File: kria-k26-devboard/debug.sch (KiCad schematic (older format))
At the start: 67 parts, among them J8 1050170001, J9 0878311420, Q10 BSS138-7-F, Q11 BSS138-7-F, Q9 BSS138-7-F, U29 MIC5211-3.3YM6-TR, U30 FT4232HPQ, U31 93LC56CT-IMC, U32 74AVC4T245RSVRG4, U33 74AVC4T245RSVRG4, U34 SN74AVC2T245RSWR, U35 SN74AVC2T245RSWR, U36 NC7WZ07P6X, Y5 ABM8G-12.000MHZ-18-D2Y-T

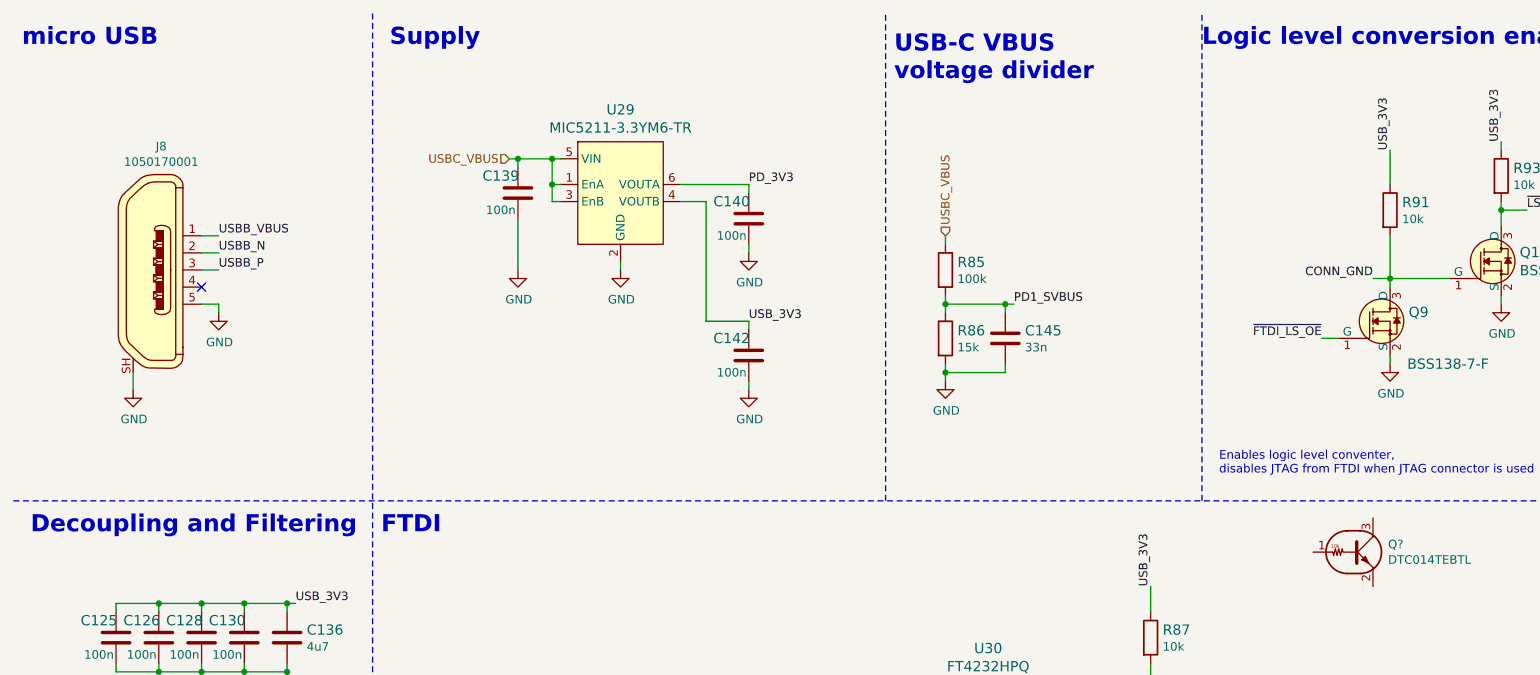
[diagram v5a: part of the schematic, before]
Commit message: Initial routing of ETH and USB 2.0 interface, debug socket USB replaced to USB-C, added stud for M2
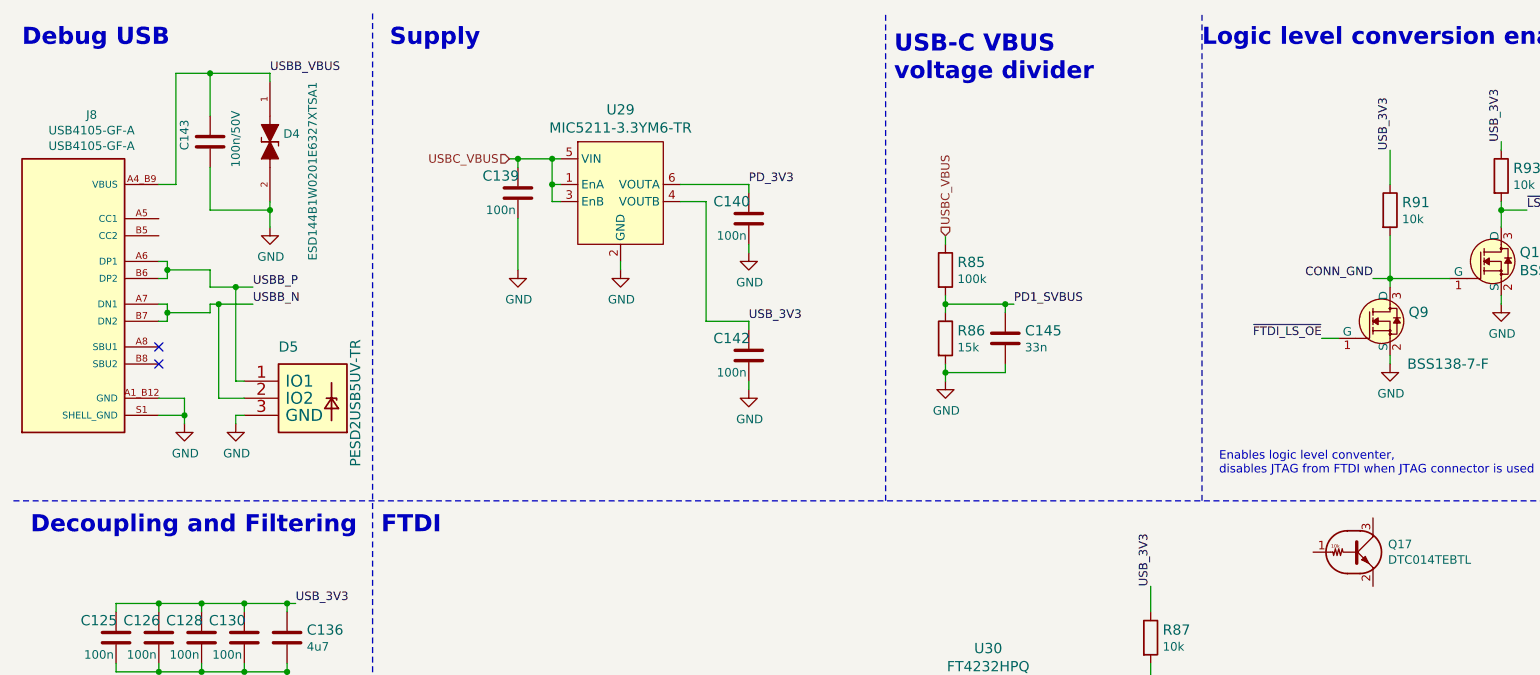
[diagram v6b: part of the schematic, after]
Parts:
- removed J8: 1050170001, antmicro-footprints:USB_Micro_B_Female_1050170001, symbol antmicroUSBDVIHDMIConnectors:1050170001
- added C143: C_100n_0402_50V, antmicro-footprints:0402-cap, symbol antmicroCapacitorsmisc:C_100n_0402_50V
- added D4: ESD144B1W0201E6327XTSA1, antmicro-footprints:ESD144B1W0201E6327XTSA1, symbol antmicroTVSDiodes:ESD144B1W0201E6327XTSA1
- added D5: PESD2USB5UV-TR, antmicro-footprints:SOT-23s, symbol antmicroTVSDiodes:PESD2USB5UV-TR
- added J8: USB4105-GF-A, antmicro-footprints:GCT_USB4105-GF-A, symbol antmicroUSBDVIHDMIConnectors:USB4105-GF-A
- gave numbers to parts that had none: 1
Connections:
- net GND: now also C143.2, D4.2, D5.3 (GND), J8.A1_B12 (GND), J8.B1_A12 (GND), J8.S1 (SHELL_GND), J8.S2 (SHELL_GND), J8.S3 (SHELL_GND), J8.S4 (SHELL_GND)
- net USBB_N: now also D5.2 (IO2), J8.A7 (DN1), J8.B7 (DN2)
- net USBB_P: now also D5.1 (IO1), J8.A6 (DP1), J8.B6 (DP2)
- net USBB_VBUS renamed VBUS
- net VBUS: now also C143.1, D4.1, J8.A4_B9 (VBUS), J8.B4_A9 (VBUS)
- no-connect marks 34 -> 35
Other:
- note added: "Debug USB"
- note removed: "micro USB"
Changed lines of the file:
@@
 Text Label 4600 6950 2    50   ~ 0
 USB_N
-Text Label 1700 1800 0    50   ~ 0
-USBB_VBUS
-Wire Wire Line
-	1600 1800 1700 1800
-NoConn ~ 1600 2100
-$Comp
-L power:GND #PWR?
-U 1 1 6602D48C
-P 1700 2250
-AR Path="/63C44BC2/6602D48C" Ref="#PWR?"  Part="1"
-AR Path="/63C44BC2/6235D136/6602D48C" Ref="#PWR?"  Part="1"
-AR Path="/63C44BC2/623E44F4/6602D48C" Ref="#PWR?"  Part="1"
-AR Path="/63C44BC2/6244F9D5/6602D48C" Ref="#PWR?"  Part="1"
-AR Path="/625B0244/6602D48C" Ref="#PWR0299"  Part="1"
-F 0 "#PWR0299" H 1700 2000 50  0001 C CNN
-F 1 "GND" H 1705 2077 50  0000 C CNN
-F 2 "" H 1700 2250 50  0001 C CNN
-F 3 "" H 1700 2250 50  0001 C CNN
-	1    1700 2250
-	1    0    0    -1
-$EndComp
-Wire Wire Line
-	1600 2200 1700 2200
-Wire Wire Line
-	1700 2200 1700 2250
-$Comp
-L power:GND #PWR?
-U 1 1 66051E26
-P 1200 2700
-AR Path="/63C44BC2/66051E26" Ref="#PWR?"  Part="1"
-AR Path="/63C44BC2/6235D136/66051E26" Ref="#PWR?"  Part="1"
-AR Path="/63C44BC2/623E44F4/66051E26" Ref="#PWR?"  Part="1"
-AR Path="/63C44BC2/6244F9D5/66051E26" Ref="#PWR?"  Part="1"
-AR Path="/625B0244/66051E26" Ref="#PWR0298"  Part="1"
-F 0 "#PWR0298" H 1200 2450 50  0001 C CNN
-F 1 "GND" H 1205 2527 50  0000 C CNN
-F 2 "" H 1200 2700 50  0001 C CNN
-F 3 "" H 1200 2700 50  0001 C CNN
-	1    1200 2700
-	1    0    0    -1
-$EndComp
-Wire Wire Line
-	1200 2700 1200 2600
-Text Label 1700 2000 0    50   ~ 0
-USBB_P
-Wire Wire Line
-	1600 2000 1700 2000
-Text Label 1700 1900 0    50   ~ 0
-USBB_N
-Wire Wire Line
-	1600 1900 1700 1900
 Text Label 3250 10450 0    50   ~ 0
 USBB_P
@@
 Connector configuration
 Text Notes 550  700  0    100  ~ 20
-micro USB
+Debug USB
 Text Notes 2700 700  0    100  ~ 20
 Supply
@@
 NoConn ~ 7000 7700
 NoConn ~ 7000 7800
-$Comp
-L antmicroUSBDVIHDMIConnectors:1050170001 J8
-U 1 1 6B83F4A7
-P 1300 2000
-F 0 "J8" H 1364 2723 50  0000 C CNN
-F 1 "1050170001" H 1364 2632 50  0000 C CNN
-F 2 "antmicro-footprints:USB_Micro_B_Female_1050170001" H 1500 2200 60  0001 L CNN
-F 3 "https://www.molex.com/pdm_docs/sd/1050170001_sd.pdf" H 1500 2300 60  0001 L CNN
-F 4 "1050170001" H 1500 2500 60  0001 L CNN "MPN"
-F 5 "Molex" H 1500 3100 60  0001 L CNN "Manufacturer"
-	1    1300 2000
-	1    0    0    -1
-$EndComp
 Text Notes 12200 4350 0    50   ~ 0
 2 A <- B
@@
 	3650 1600 3700 1600
 Connection ~ 3650 1500
-Wire Bus Line
-	4700 6500 4700 6700
-$Comp
-L antmicroTransistorsBipolarSingle:DTC014TEBTL Q?
+$Comp
+L antmicroTransistorsBipolarSingle:DTC014TEBTL Q17
 U 1 1 63983E69
 P 8350 3650
-F 0 "Q?" H 8538 3696 50  0000 L CNN
+F 0 "Q17" H 8538 3696 50  0000 L CNN
 F 1 "DTC014TEBTL" H 8538 3605 50  0000 L CNN
 F 2 "antmicro-footprints:SOT-416" H 8550 3350 50  0001 L CNN
@@
 	1    0    0    -1
 $EndComp
+Text Label 2000 850  0    50   ~ 0
+USBB_VBUS
+Connection ~ 1500 2850
+Wire Wire Line
+	1500 2900 1500 2850
+$Comp
+L power:GND #PWR?
+U 1 1 6424D92A
+P 1500 2900
+AR Path="/63C44BC2/6424D92A" Ref="#PWR?"  Part="1"
+AR Path="/63C44BC2/62A9ECDC/6424D92A" Ref="#PWR?"  Part="1"
+AR Path="/625B0244/6424D92A" Ref="#PWR0298"  Part="1"
+F 0 "#PWR0298" H 1500 2650 50  0001 C CNN
+F 1 "GND" H 1505 2727 50  0000 C CNN
+F 2 "" H 1500 2900 50  0001 C CNN
+F 3 "" H 1500 2900 50  0001 C CNN
+	1    1500 2900
+	1    0    0    -1
+$EndComp
+Wire Wire Line
+	1500 2850 1350 2850
+Wire Wire Line
+	1500 2750 1500 2850
+Wire Wire Line
+	1350 2750 1500 2750
+Wire Wire Line
+	1400 2300 1350 2300
+Wire Wire Line
+	1350 2200 1400 2200
+Wire Wire Line
+	1400 2050 1350 2050
+Wire Wire Line
+	1350 1950 1400 1950
+$Comp
+L antmicroTVSDiodes:ESD144B1W0201E6327XTSA1 D?
+U 1 1 6424D93B
+P 2000 1250
+AR Path="/63C44BC2/6424D93B" Ref="D?"  Part="1"
+AR Path="/63C44BC2/62A9ECDC/6424D93B" Ref="D?"  Part="1"
+AR Path="/625B0244/6424D93B" Ref="D4"  Part="1"
+F 0 "D4" V 1954 1328 50  0000 L CNN
+F 1 "ESD144B1W0201E6327XTSA1" H 1650 1500 50  0000 L CNN
+F 2 "antmicro-footprints:ESD144B1W0201E6327XTSA1" H 2000 1250 50  0001 C CNN
+F 3 "https://www.infineon.com/dgdl/Infineon-ESD144-B1-W0201-DataSheet-v02_00-EN.pdf?fileId=5546d462677d0f4601679886a2a8707c" H 2000 1250 50  0001 C CNN
+F 4 "ESD144B1W0201E6327XTSA1" H 2000 1250 50  0001 C CNN "MPN"
+F 5 "Infineon Technologies" H 2000 1250 50  0001 C CNN "Manufacturer"
+	1    2000 1250
+	0    1    1    0
+$EndComp
+$Comp
+L power:GND #PWR?
+U 1 1 6424D942
+P 2000 1750
+AR Path="/63C44BC2/6424D942" Ref="#PWR?"  Part="1"
+AR Path="/63C44BC2/62A9ECDC/6424D942" Ref="#PWR?"  Part="1"
+AR Path="/625B0244/6424D942" Ref="#PWR0299"  Part="1"
+F 0 "#PWR0299" H 2000 1500 50  0001 C CNN
+F 1 "GND" H 2005 1577 50  0000 C CNN
+F 2 "" H 2000 1750 50  0001 C CNN
+F 3 "" H 2000 1750 50  0001 C CNN
+	1    2000 1750
+	1    0    0    -1
+$EndComp
+NoConn ~ 1350 2550
+NoConn ~ 1350 2450
+$Comp
+L antmicroCapacitorsmisc:C_100n_0402_50V C?
+U 1 1 6424D94D
+P 1650 1250
+AR Path="/63C44BC2/6424D94D" Ref="C?"  Part="1"
+AR Path="/63C44BC2/62A9ECDC/6424D94D" Ref="C?"  Part="1"
+AR Path="/625B0244/6424D94D" Ref="C143"  Part="1"
+F 0 "C143" V 1500 1200 50  0000 L CNN
+F 1 "C_100n_0402_50V" H 1650 1250 50  0001 C CNN
+F 2 "antmicro-footprints:0402-cap" H 1650 1250 50  0001 C CNN
+F 3 "" H 1650 1250 50  0001 C CNN
+F 4 "GRM155R71H104KE14D" H 1650 1250 50  0001 C CNN "MPN"
+F 5 "MURATA" H 1650 1250 50  0001 C CNN "Manufacturer"
+F 6 "100n/50V" V 1800 1100 50  0000 L CNN "Val"
+	1    1650 1250
+	1    0    0    -1
+$EndComp
+Wire Wire Line
+	2000 850  1650 850
+Wire Wire Line
+	1650 850  1650 1100
+Wire Wire Line
+	2000 850  2000 900
+Wire Wire Line
+	2000 1600 2000 1650
+Wire Wire Line
+	1650 1650 2000 1650
+Wire Wire Line
+	1650 1400 1650 1650
+Connection ~ 2000 1650
+Wire Wire Line
+	2000 1650 2000 1750
+$Comp
+L antmicroTVSDiodes:PESD2USB5UV-TR D?
+U 1 1 6424D95D
+P 2050 2650
+AR Path="/63C44BC2/6424D95D" Ref="D?"  Part="1"
+AR Path="/63C44BC2/62A9ECDC/6424D95D" Ref="D?"  Part="1"
+AR Path="/625B0244/6424D95D" Ref="D5"  Part="1"
+F 0 "D5" H 2050 2850 60  0000 L CNN
+F 1 "PESD2USB5UV-TR" V 2500 2150 60  0000 L CNN
+F 2 "antmicro-footprints:SOT-23s" H 2100 2850 60  0001 C CNN
+F 3 "https://assets.nexperia.com/documents/data-sheet/PESD2USB5UV-T.pdf" H 2050 2650 60  0001 C CNN
+F 4 "PESD2USB5UV-TR " H 1750 2950 50  0001 C CNN "MPN"
+F 5 "Nexperia " H 1750 3050 50  0001 C CNN "Manufacturer"
+	1    2050 2650
+	1    0    0    -1
+$EndComp
+$Comp
+L power:GND #PWR?
+U 1 1 6424D963
+P 1800 2900
+AR Path="/63C44BC2/6424D963" Ref="#PWR?"  Part="1"
+AR Path="/63C44BC2/62A9ECDC/6424D963" Ref="#PWR?"  Part="1"
+AR Path="/625B0244/6424D963" Ref="#PWR0306"  Part="1"
+F 0 "#PWR0306" H 1800 2650 50  0001 C CNN
+F 1 "GND" H 1805 2727 50  0000 C CNN
+F 2 "" H 1800 2900 50  0001 C CNN
+F 3 "" H 1800 2900 50  0001 C CNN
+	1    1800 2900
+	1    0    0    -1
+$EndComp
+Wire Wire Line
+	1800 2900 1800 2850
+Wire Wire Line
+	1800 2850 1850 2850
+Wire Wire Line
+	1850 2750 1700 2750
+Wire Wire Line
+	1400 2200 1400 2250
+Wire Wire Line
+	1400 1950 1400 2000
+Wire Wire Line
+	1400 2000 1650 2000
+Connection ~ 1400 2000
+Wire Wire Line
+	1400 2000 1400 2050
+Connection ~ 1400 2250
+Wire Wire Line
+	1400 2250 1400 2300
+Wire Wire Line
+	1350 1500 1450 1500
+Wire Wire Line
+	1450 850  1650 850
+Wire Wire Line
+	1450 850  1450 1500
+Connection ~ 1650 850
+$Comp
+L antmicroUSBDVIHDMIConnectors:USB4105-GF-A J?
+U 1 1 6424D98C
+P 550 2450
+AR Path="/63C44BC2/6424D98C" Ref="J?"  Part="1"
+AR Path="/63C44BC2/62A9ECDC/6424D98C" Ref="J?"  Part="1"
+AR Path="/625B0244/6424D98C" Ref="J8"  Part="1"
+F 0 "J8" H 957 3807 50  0000 C CNN
+F 1 "USB4105-GF-A" H 957 3716 50  0000 C CNN
+F 2 "antmicro-footprints:GCT_USB4105-GF-A" H -100 2700 50  0001 L BNN
+F 3 "https://gct.co/files/drawings/usb4105.pdf" H 550 2450 50  0001 L BNN
+F 4 "GCT" H -100 2800 50  0001 L BNN "Manufacturer"
+F 5 "USB4105-GF-A" H 957 3625 50  0000 C CNN "MPN"
+	1    550  2450
+	1    0    0    -1
+$EndComp
+Wire Wire Line
+	1900 2200 1700 2200
+Wire Wire Line
+	1650 2250 1650 2200
+Wire Wire Line
+	1400 2250 1650 2250
+Wire Wire Line
+	1650 2000 1650 2100
+Text Label 1900 2200 0    50   ~ 0
+USBB_N
+Text Label 1900 2100 0    50   ~ 0
+USBB_P
+Wire Wire Line
+	1800 2650 1800 2100
+Connection ~ 1800 2100
+Wire Wire Line
+	1800 2100 1900 2100
+Wire Wire Line
+	1800 2650 1850 2650
+Wire Wire Line
+	1650 2100 1800 2100
+Wire Wire Line
+	1700 2200 1700 2750
+Connection ~ 1700 2200
+Wire Wire Line
+	1700 2200 1650 2200
+Wire Bus Line
+	4700 6500 4700 6700
 $EndSCHEMATC
